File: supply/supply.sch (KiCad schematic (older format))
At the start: 47 parts

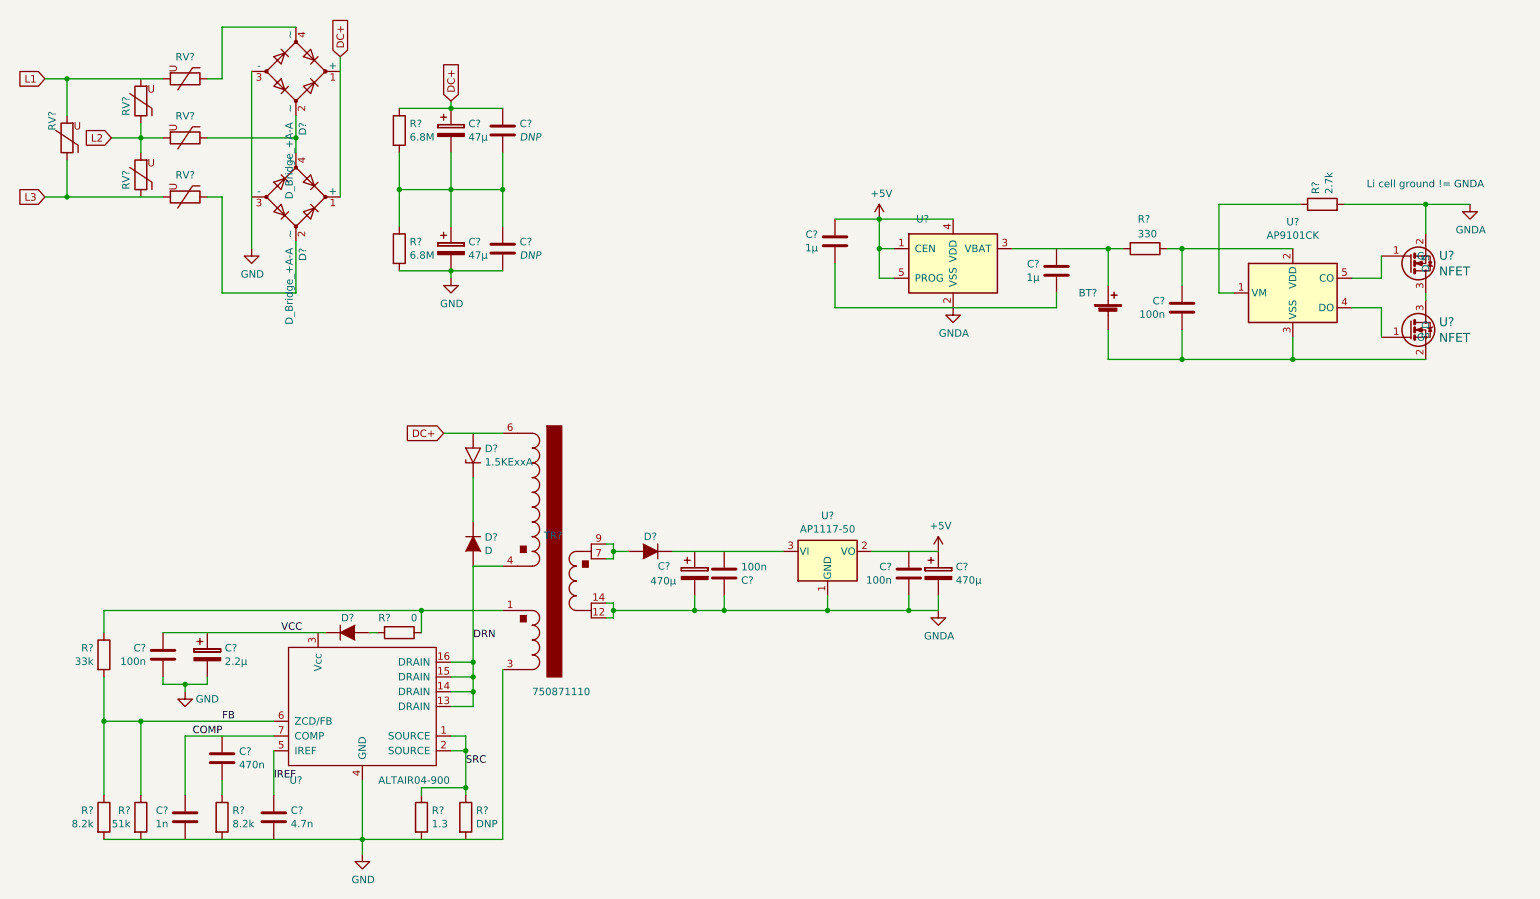
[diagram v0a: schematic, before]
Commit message: move fuses, add power header
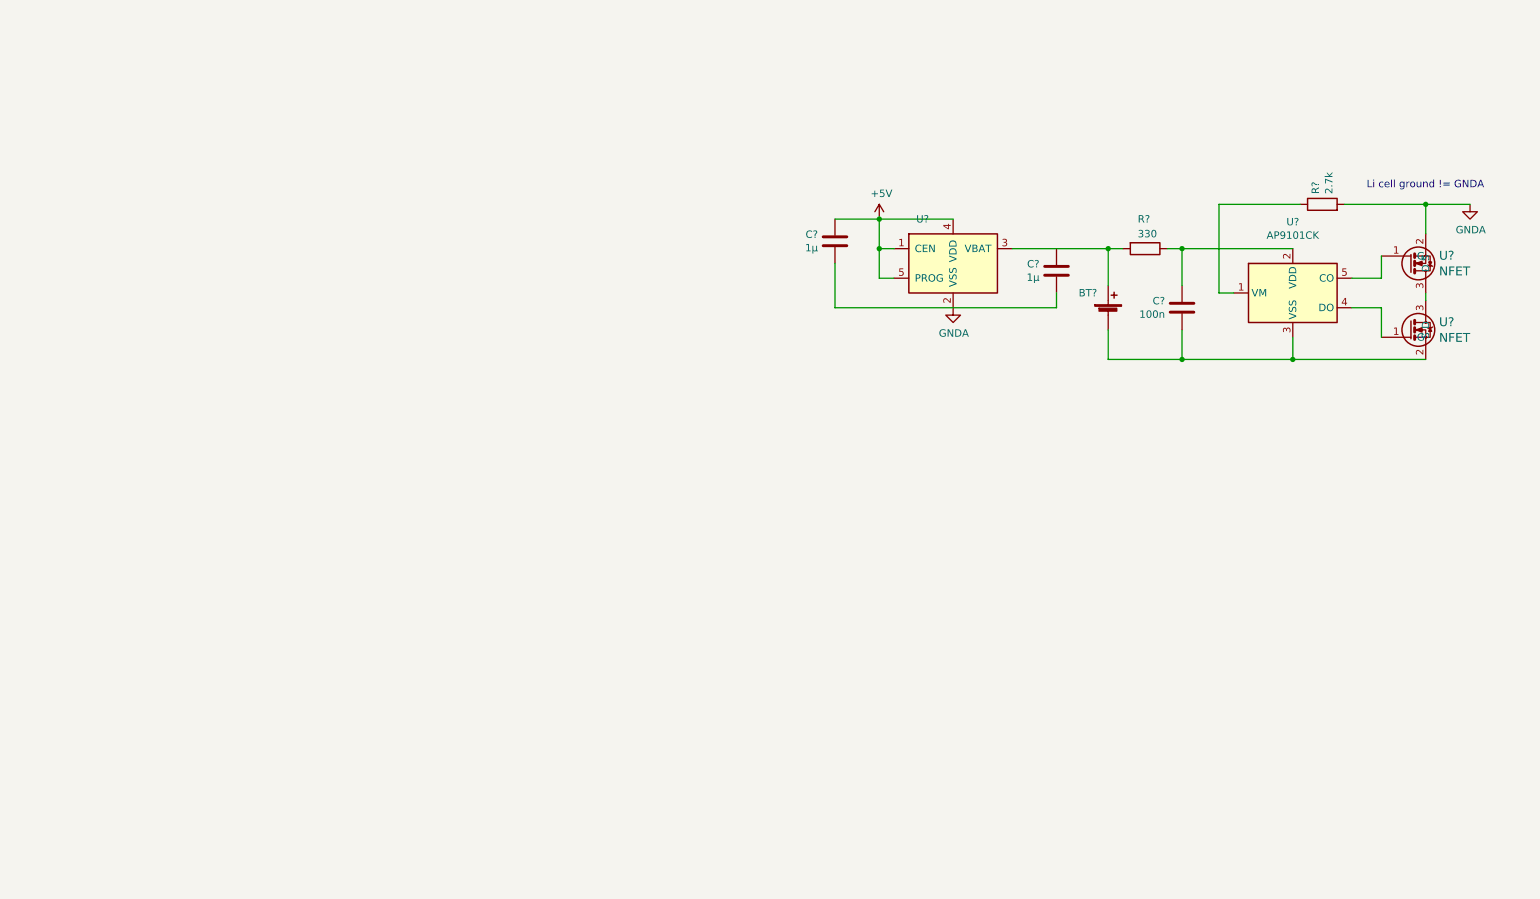
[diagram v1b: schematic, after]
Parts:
- removed C? (x2): DNP, symbol stmbl:C
- removed C? (x2): 47µ, Capacitor_THT:CP_Radial_D12.5mm_P5.00mm, symbol stmbl:CP
- removed C?: 470µ, Capacitor_SMD:CP_Elec_8x10, symbol stmbl:CP
- removed C? (x3): 100n, stmbl:C_0805, symbol stmbl:C
- removed C?: 470µ, Capacitor_SMD:CP_Elec_8x10.5, symbol stmbl:CP
- removed C?: 470n, stmbl:C_0805, symbol stmbl:C
- removed C?: 4.7n, stmbl:C_0805, symbol stmbl:C
- removed C?: 1n, stmbl:C_0805, symbol stmbl:C
- removed C?: 2.2µ, Capacitors_SMD:CP_Elec_6.3x4.5, symbol stmbl:CP
- removed D? (x3): D, stmbl:SMA_Standard, symbol stmbl:D
- removed D?: 1.5KExxA, stmbl:SMA_Standard, symbol Diode:1.5KExxA
- removed D? (x2): D_Bridge_+A-A, Diodes_SMD:Diode_Bridge_MBLS, symbol Device:D_Bridge_+A-A
- removed R? (x2): 6.8M, stmbl:R_1206, symbol stmbl:R
- removed R?: 1.3, stmbl:R_1206, symbol stmbl:R
- removed R?: DNP, stmbl:R_1206, symbol stmbl:R
- removed R? (x2): 8.2k, stmbl:R_0805, symbol stmbl:R
- removed R?: 51k, stmbl:R_0805, symbol stmbl:R
- removed R?: 33k, stmbl:R_0805, symbol stmbl:R
- removed R?: 0, stmbl:R_0805, symbol stmbl:R
- removed RV? (x6): Varistor, Varistor:RV_Disc_D12mm_W4.5mm_P7.5mm, symbol Device:Varistor
- removed TR?: 750871110, altair04:750871110, symbol altair04:TRANSFO
- removed U?: AP1117-50, Package_TO_SOT_SMD:SOT-223-3_TabPin2, symbol Regulator_Linear:AP1117-50
- removed U?: ALTAIR04-900, Package_SO:SOIC-16_3.9x9.9mm_P1.27mm, symbol altair04:ALTAIR04-900
